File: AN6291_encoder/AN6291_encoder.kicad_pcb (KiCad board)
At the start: 2 copper layers, 89.3 x 58 mm, 130 parts, among them IC1 TPS70960DBVT, J1 input mic, J2 output, J3 batt, J4 input line, Q1 NPN, Q2 NPN, Q3 BC848, Q4 BCV62, Q5 BCV62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

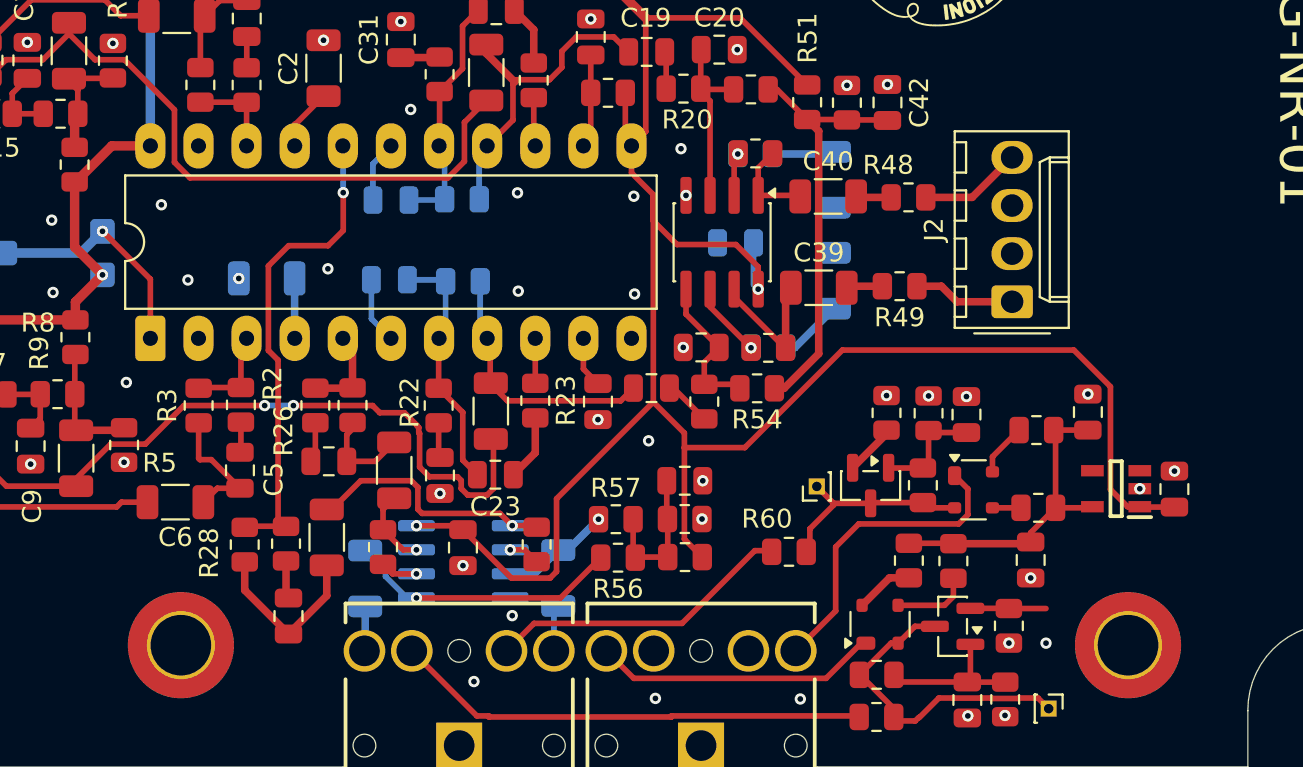
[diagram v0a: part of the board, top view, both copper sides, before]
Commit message: Removed voltage regulator for microphone supply now powered from 9v battery for lower noise
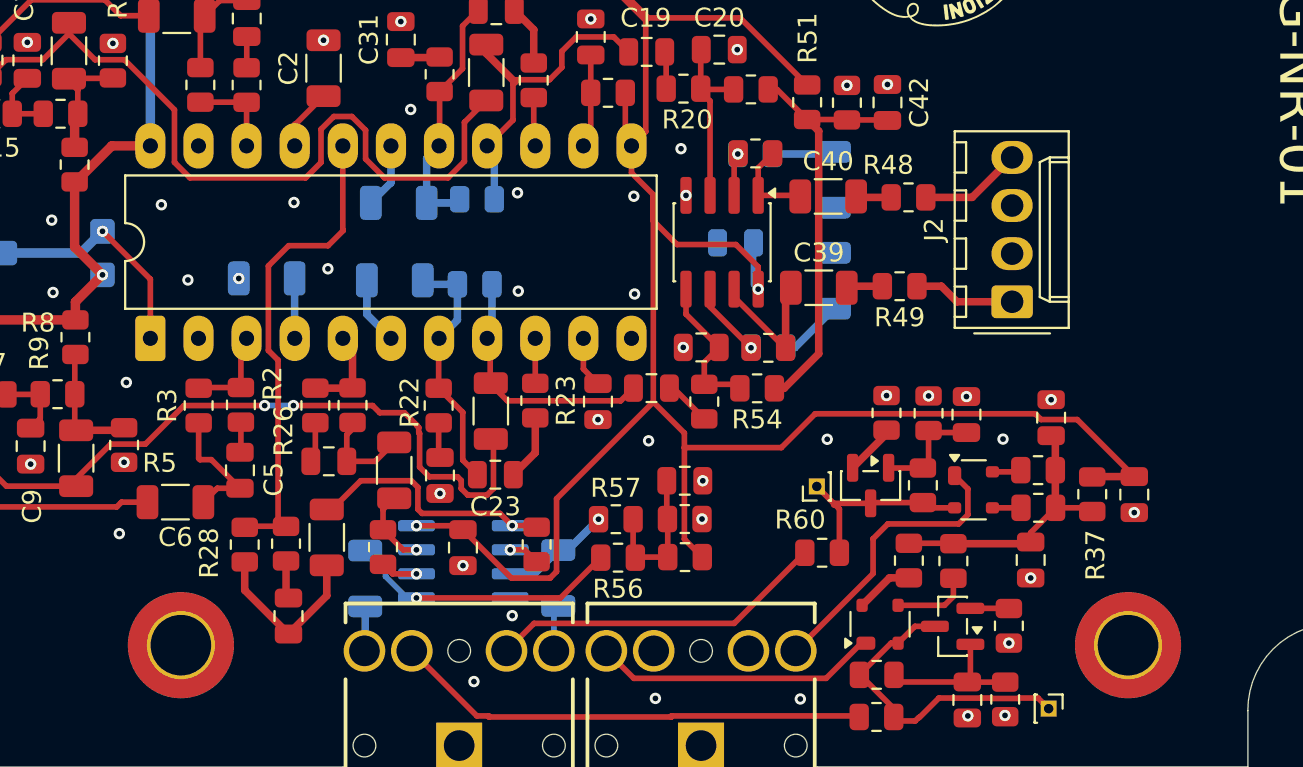
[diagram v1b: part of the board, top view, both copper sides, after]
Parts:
- removed IC1: TPS70960DBVT, LIB_TPS70960DBVT:SOT95P280X145-5N
- added R37: 100R, Resistor_SMD:R_0805_2012Metric, F.Cu at (172.2, 101.0)
- C20: value 10nf np -> 10nf COG
- C22: value 10nf NP -> 10nf COG
- C24, C30: footprint Capacitor_SMD:C_0805_2012Metric -> Capacitor_SMD:C_1206_3216Metric
- moved C36 2.14 mm to (174.4, 101.0), turned to 90 degrees
- moved R40 2.12 mm to (169.3, 99.8)
- moved C35 1.96 mm to (170.0, 97.0)
- moved R60 1.75 mm to (157.9, 104.1)
- moved R31 0.80 mm to (139.7, 85.5)
- moved R24 0.64 mm to (139.6, 90.0)
- moved C30 0.44 mm to (135.6, 85.7)
- moved C24 0.28 mm to (135.4, 89.7)
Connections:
- net +6V renamed 9V mic
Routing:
- net VCC: track 202.2 -> 195.7 mm
- net Net-(C12-Pad1): track 35.5 -> 40.1 mm
- net Net-(Q3-E): track 3.98 -> 2.02 mm
- net 9V mic: track 16.6 -> 14.7 mm
- net Net-(J4-Pad4): track 16.4 -> 17.9 mm
- net Net-(Q5-E2): track 2.79 -> 1.53 mm
- net /mic in Sx: track 16.4 -> 15.5 mm
- net Net-(U1-VOUT–_B): track 16.8 -> 17.4 mm
- net Net-(U1-CAP_2–_A): track 12.6 -> 13.2 mm
- net Net-(U1-CCA_IN–B): vias 1 -> 0
- net GND: vias 52 -> 54

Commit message: rev B
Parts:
- R33, R35, R40, R42: value 274R -> 270R
- R34, R39: value 57,6K -> 56k
- R48, R49, R58, R59: value 100 -> 100R
